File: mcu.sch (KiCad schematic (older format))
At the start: 36 parts, among them J10 USB_C_Receptacle_USB2.0, J4 debug, J5 Conn_01x16_Male, J6 Conn_01x16_Male, SW1 SW_MEC_5E, SW2 SW_MEC_5E, U3 STM32F407VETx, Y1 12Mhz

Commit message: Add debug interface
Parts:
- removed J4: debug, symbol Connector_Generic:Conn_01x07
- added J10: debug, symbol Connector_Generic:Conn_01x06
- renumbered C18 to C10, C19 to C11, C20 to C12, C21 to C13, C22 to C14, C23 to C15, C24 to C16, C25 to C17, C26 to C18, C27 to C19, C28 to C20, C30 to C6, C16 to C7, C31 to C8, C17 to C9, D1 to D5, D2 to D6, D3 to D7, D4 to D8, J5 to J7, J6 to J8, J10 to J9, R16 to R10, R17 to R11, R11 to R12, R12 to R13, R13 to R14, R7 to R15, R8 to R16, R9 to R17, R10 to R18
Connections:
- net labels removed: JTDI, NJTRST
- wire segments 210 -> 206
- no-connect marks 2 -> 3

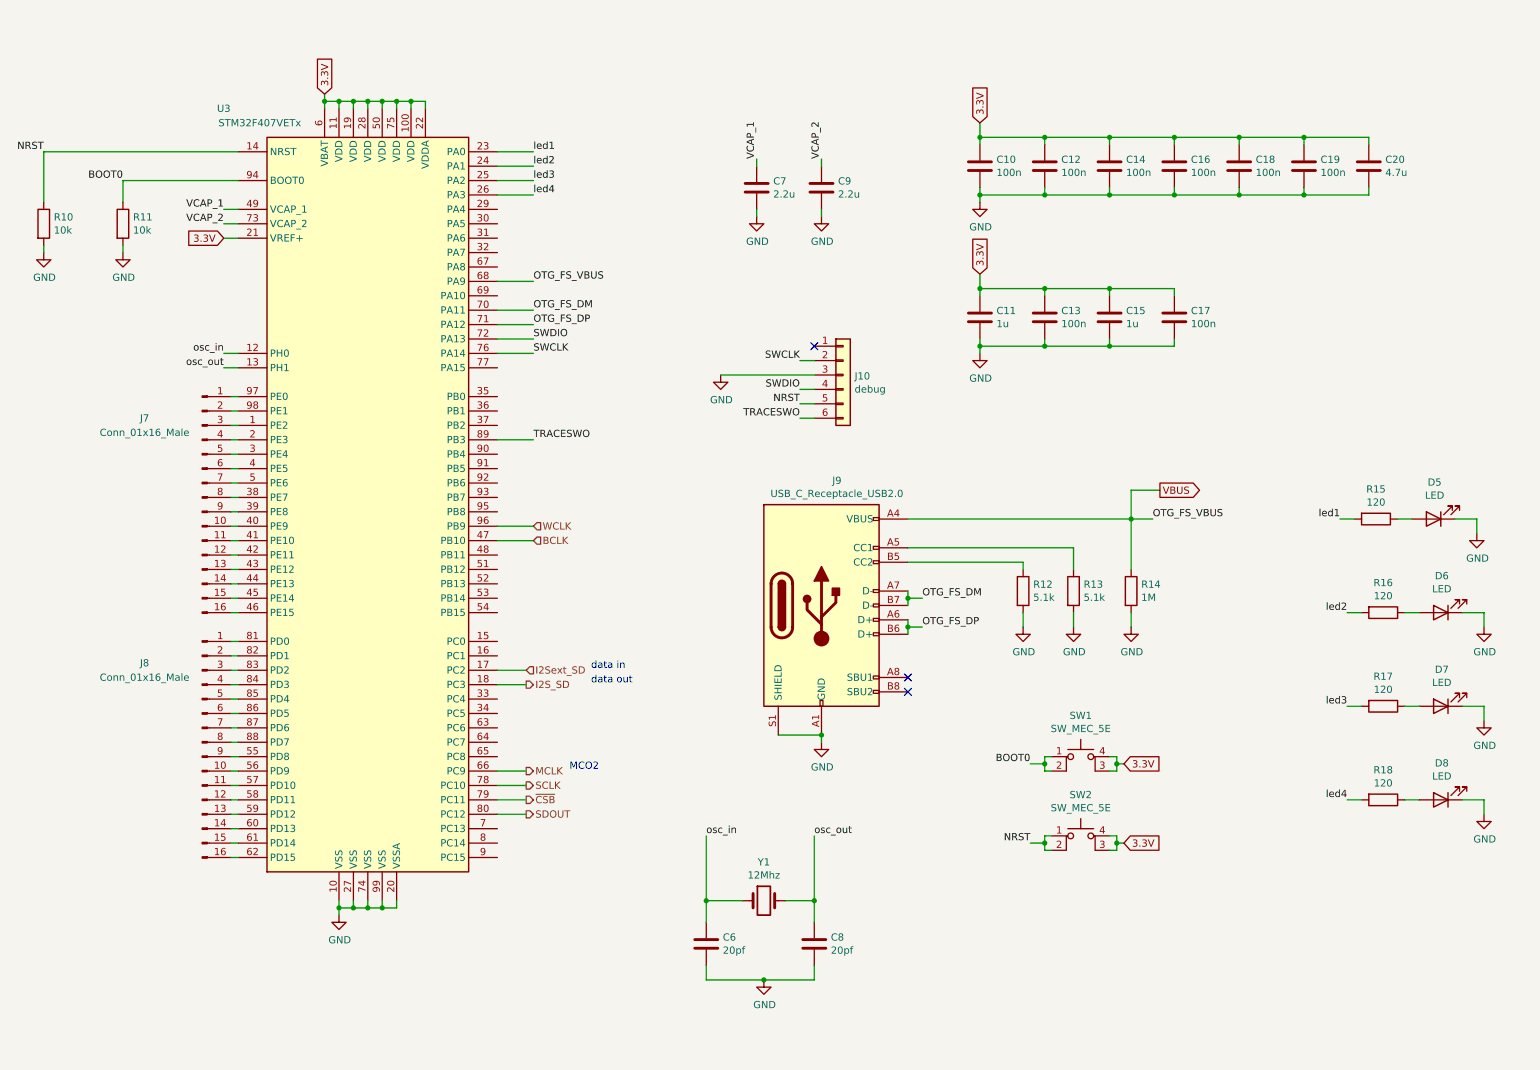
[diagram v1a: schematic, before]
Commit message: Add traces
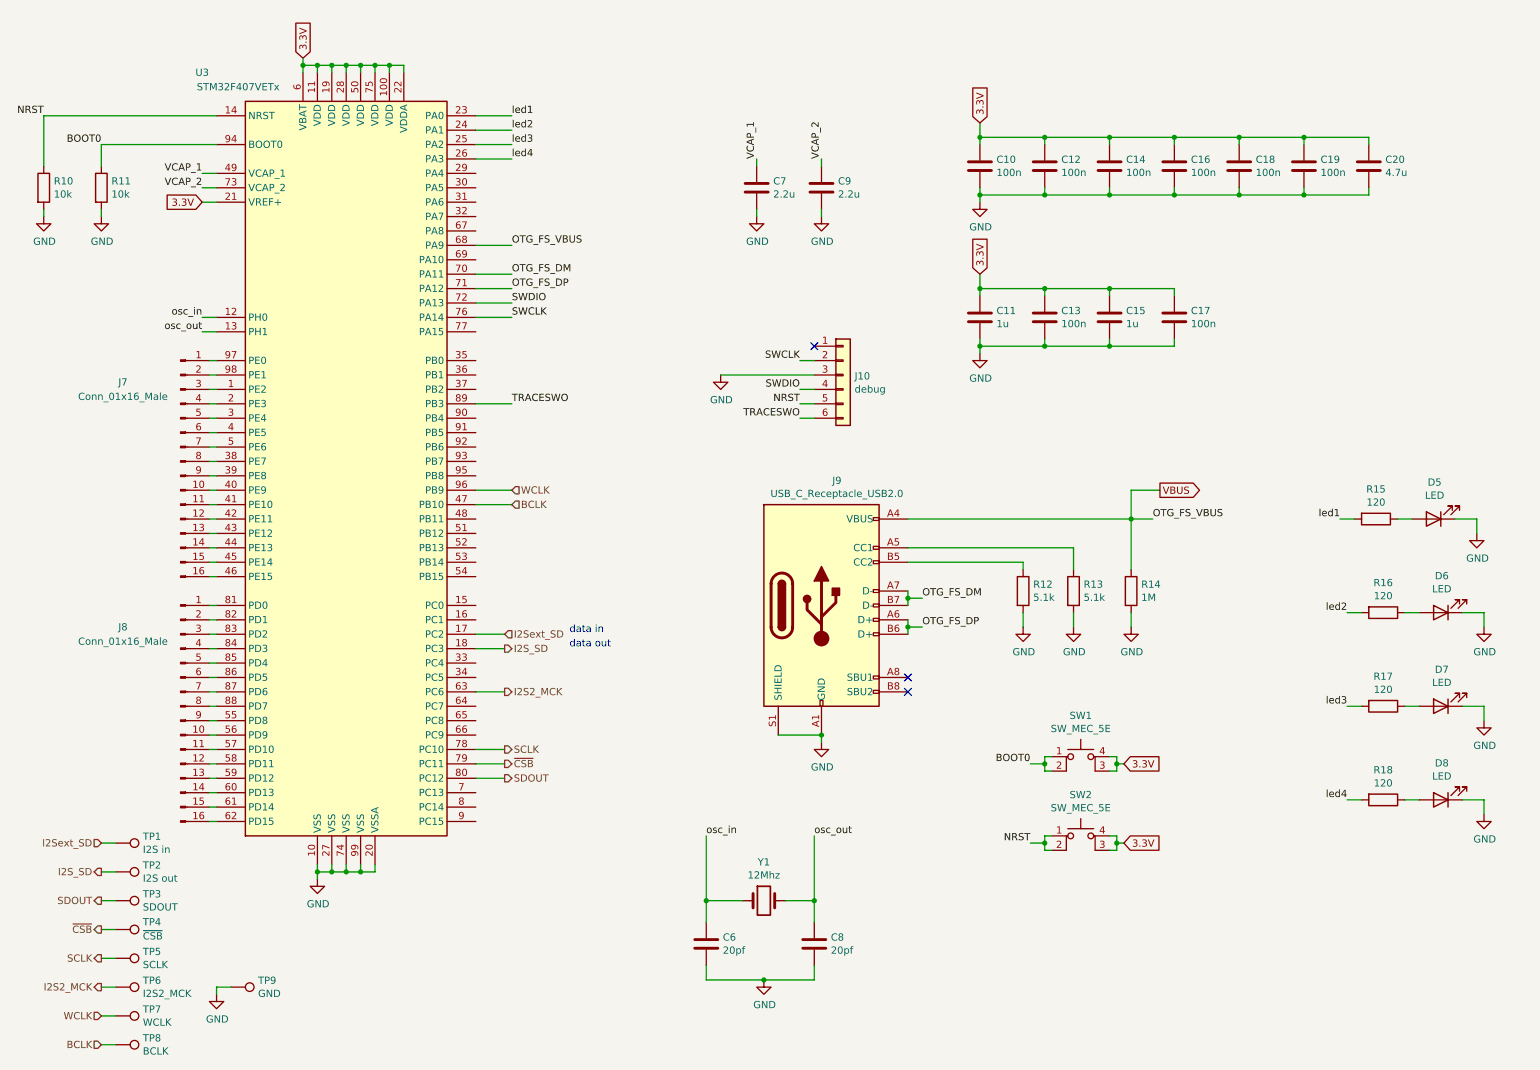
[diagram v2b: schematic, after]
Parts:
- added TP1: I2S in, symbol Connector:TestPoint
- added TP2: I2S out, symbol Connector:TestPoint
- added TP3: SDOUT, symbol Connector:TestPoint
- added TP4: ~CSB, symbol Connector:TestPoint
- added TP5: SCLK, symbol Connector:TestPoint
- added TP6: I2S2_MCK, symbol Connector:TestPoint
- added TP7: WCLK, symbol Connector:TestPoint
- added TP8: BCLK, symbol Connector:TestPoint
- added TP9: GND, symbol Connector:TestPoint
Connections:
- net BCLK: now also TP8.1
- net GND: now also TP9.1
- net I2S_SD: now also TP2.1
- net I2Sext_SD: now also TP1.1
- net SCLK: now also TP5.1
- net SDOUT: now also TP3.1
- net WCLK: now also TP7.1
- net ~CSB: now also TP4.1
- net I2S2_MCK: now reaches U3.63 (PC6)
- net I2S2_MCK: now also TP6.1
- net MCLK: no longer names the net of U3.66 (PC9)
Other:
- note removed: "MCO2"
- moved on the sheet: J7, J8, R10, R11, U3

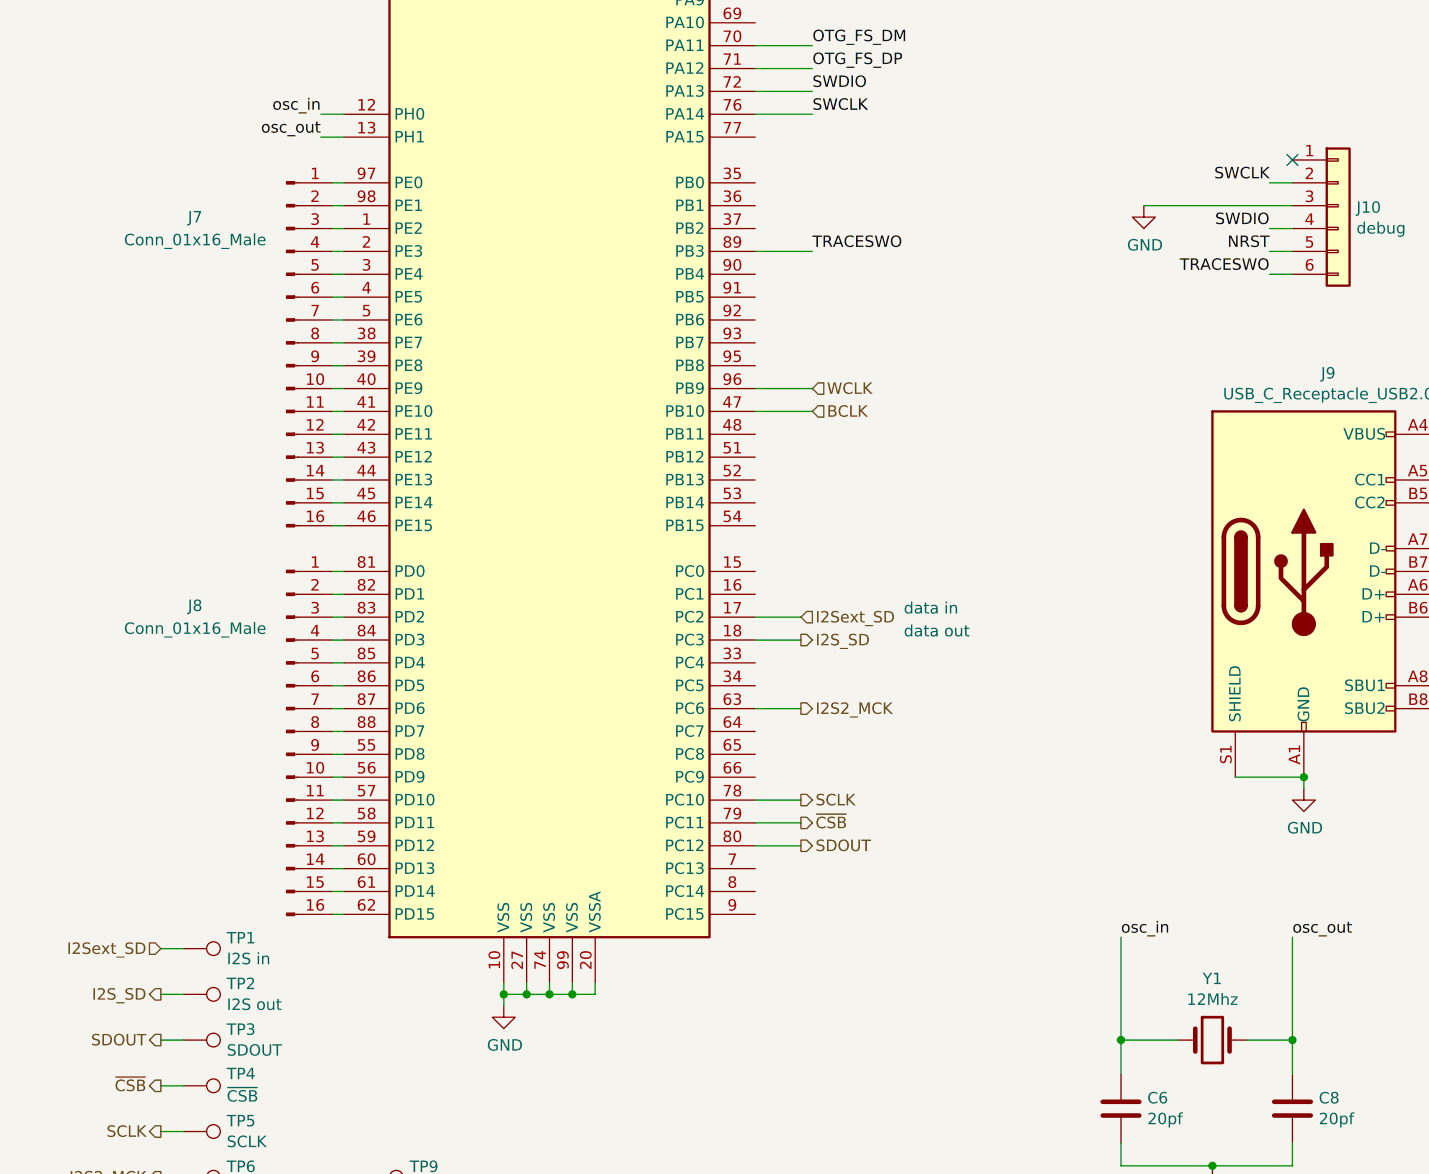
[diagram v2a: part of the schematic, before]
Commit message: Use contiguous GPIO pins
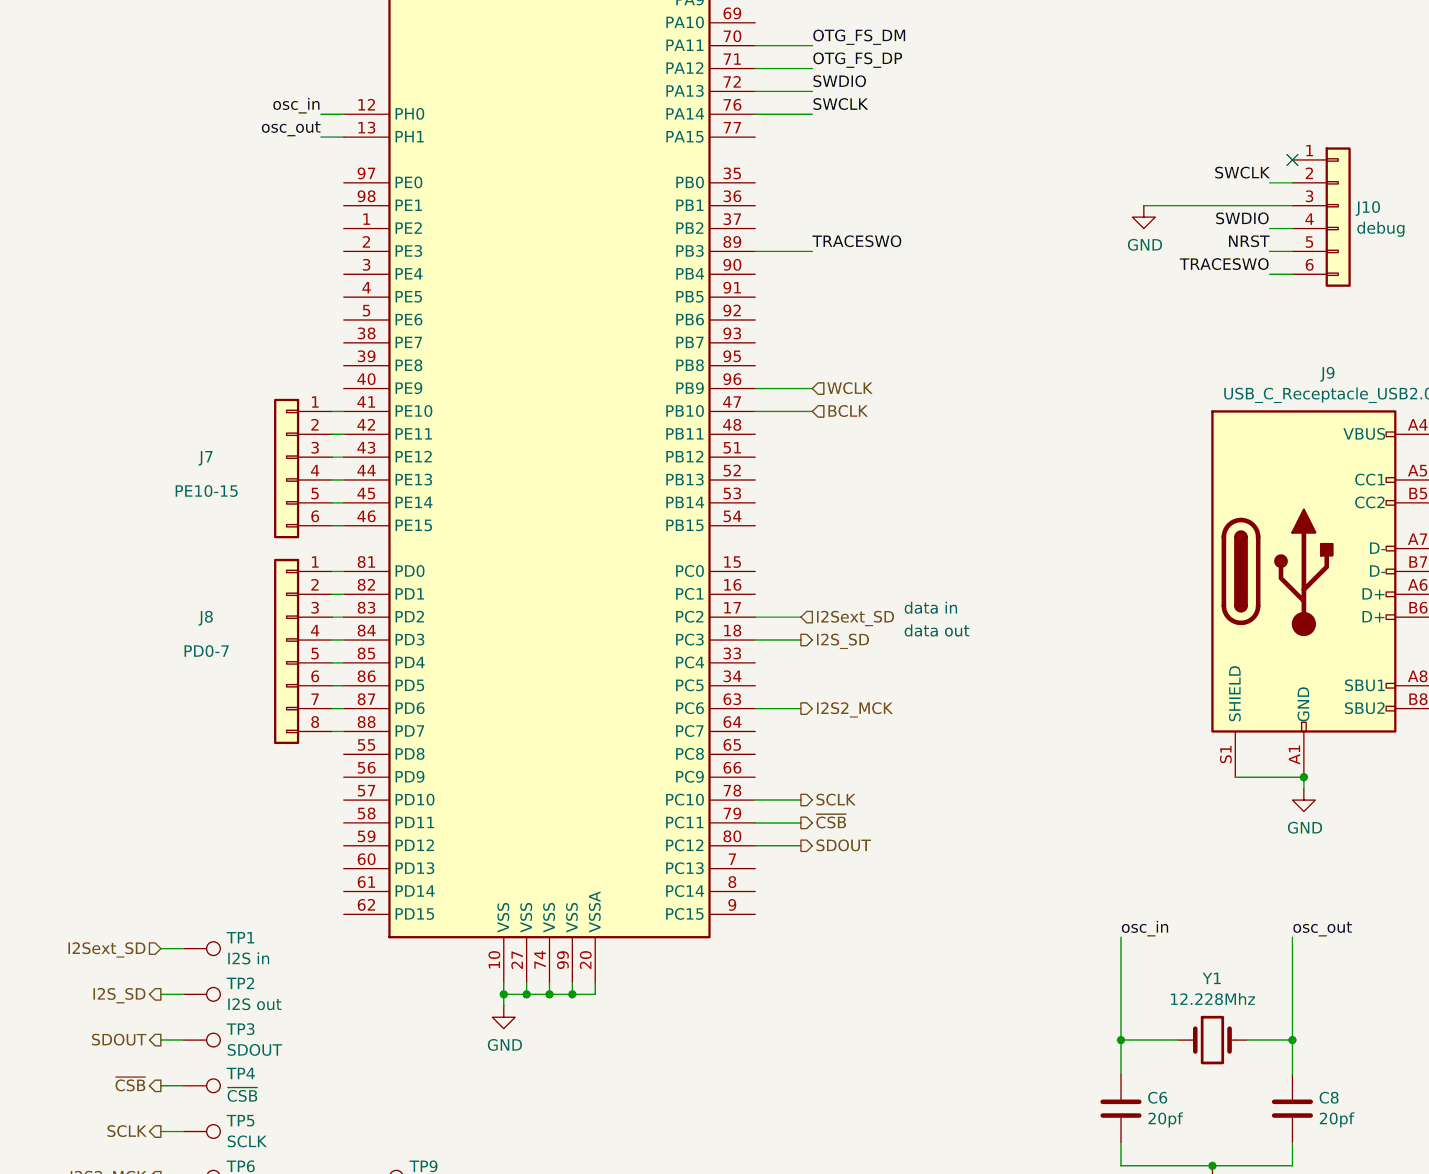
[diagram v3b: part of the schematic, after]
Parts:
- removed J7, J8: Conn_01x16_Male, symbol Connector:Conn_01x16_Male
- added J7: PE10-15, symbol Connector_Generic:Conn_01x06
- added J8: PD0-7, symbol Connector_Generic:Conn_01x08
- Y1: value 12Mhz -> 12.228Mhz
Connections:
- net at U3.41 (PE10): now also J7.1 (Pin_1)
- net at U3.42 (PE11): now also J7.2 (Pin_2)
- net at U3.43 (PE12): now also J7.3 (Pin_3)
- net at U3.44 (PE13): now also J7.4 (Pin_4)
- net at U3.45 (PE14): now also J7.5 (Pin_5)
- net at U3.46 (PE15): now also J7.6 (Pin_6)
- net at U3.81 (PD0): now also J8.1 (Pin_1)
- net at U3.82 (PD1): now also J8.2 (Pin_2)
- net at U3.83 (PD2): now also J8.3 (Pin_3)
- net at U3.84 (PD3): now also J8.4 (Pin_4)
- net at U3.85 (PD4): now also J8.5 (Pin_5)
- net at U3.86 (PD5): now also J8.6 (Pin_6)
- net at U3.87 (PD6): now also J8.7 (Pin_7)
- net at U3.88 (PD7): now also J8.8 (Pin_8)
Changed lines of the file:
@@
 P 5750 6600
 F 0 "Y1" H 5750 6868 50  0000 C CNN
-F 1 "12Mhz" H 5750 6777 50  0000 C CNN
+F 1 "12.228Mhz" H 5750 6777 50  0000 C CNN
 F 2 "" H 5750 6600 50  0001 C CNN
 F 3 "~" H 5750 6600 50  0001 C CNN
@@
 osc_in
 Wire Wire Line
-	1900 2850 1950 2850
-Wire Wire Line
-	1900 2950 1950 2950
-Wire Wire Line
-	1900 3050 1950 3050
-Wire Wire Line
-	1900 3150 1950 3150
-Wire Wire Line
-	1900 3250 1950 3250
-Wire Wire Line
-	1900 3350 1950 3350
-Wire Wire Line
-	1900 3450 1950 3450
-Wire Wire Line
-	1900 3550 1950 3550
-$Comp
-L Connector:Conn_01x16_Male J7
-U 1 1 60125863
-P 1700 3550
-F 0 "J7" H 1300 4100 50  0000 C CNN
-F 1 "Conn_01x16_Male" H 1300 4000 50  0000 C CNN
-F 2 "" H 1700 3550 50  0001 C CNN
-F 3 "~" H 1700 3550 50  0001 C CNN
-	1    1700 3550
-	1    0    0    -1
-$EndComp
-Wire Wire Line
-	1900 3650 1950 3650
-Wire Wire Line
-	1900 3750 1950 3750
-Wire Wire Line
 	1900 3850 1950 3850
 Wire Wire Line
@@
 Wire Wire Line
 	1900 4350 1950 4350
-$Comp
-L Connector:Conn_01x16_Male J8
-U 1 1 60169B70
-P 1700 5250
-F 0 "J8" H 1300 5800 50  0000 C CNN
-F 1 "Conn_01x16_Male" H 1300 5700 50  0000 C CNN
-F 2 "" H 1700 5250 50  0001 C CNN
-F 3 "~" H 1700 5250 50  0001 C CNN
-	1    1700 5250
-	1    0    0    -1
-$EndComp
 Wire Wire Line
 	1900 4550 1950 4550
@@
 Wire Wire Line
 	1900 5250 1950 5250
-Wire Wire Line
-	1900 5350 1950 5350
-Wire Wire Line
-	1900 5450 1950 5450
-Wire Wire Line
-	1900 5550 1950 5550
-Wire Wire Line
-	1900 5650 1950 5650
-Wire Wire Line
-	1900 5750 1950 5750
-Wire Wire Line
-	1900 5850 1950 5850
-Wire Wire Line
-	1900 5950 1950 5950
-Wire Wire Line
-	1900 6050 1950 6050
 $Comp
 L Device:LED D5
@@
 Text HLabel 1150 7200 0    50   Output ~ 0
 I2S2_MCK
+$Comp
+L Connector_Generic:Conn_01x08 J8
+U 1 1 605777EA
+P 1700 4850
+F 0 "J8" H 2050 4950 50  0000 C CNN
+F 1 "PD0-7" H 2050 4800 50  0000 C CNN
+F 2 "" H 1700 4850 50  0001 C CNN
+F 3 "~" H 1700 4850 50  0001 C CNN
+	1    1700 4850
+	-1   0    0    -1
+$EndComp
+$Comp
+L Connector_Generic:Conn_01x06 J7
+U 1 1 605B10FE
+P 1700 4050
+F 0 "J7" H 2050 4050 50  0000 C CNN
+F 1 "PE10-15" H 2050 3900 50  0000 C CNN
+F 2 "" H 1700 4050 50  0001 C CNN
+F 3 "~" H 1700 4050 50  0001 C CNN
+	1    1700 4050
+	-1   0    0    -1
+$EndComp
 $EndSCHEMATC
